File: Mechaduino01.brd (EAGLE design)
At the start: 41.9 x 41.9 mm, 64 parts, among them IC1 SAMD21G18A-AUT, IC2 AP2112K-3.3, Q1 2.5A/30V, Q2 NFET, Q3 BSS138, Q4 BSS138, U3 74AHC1G125, Y1 32,768Khz

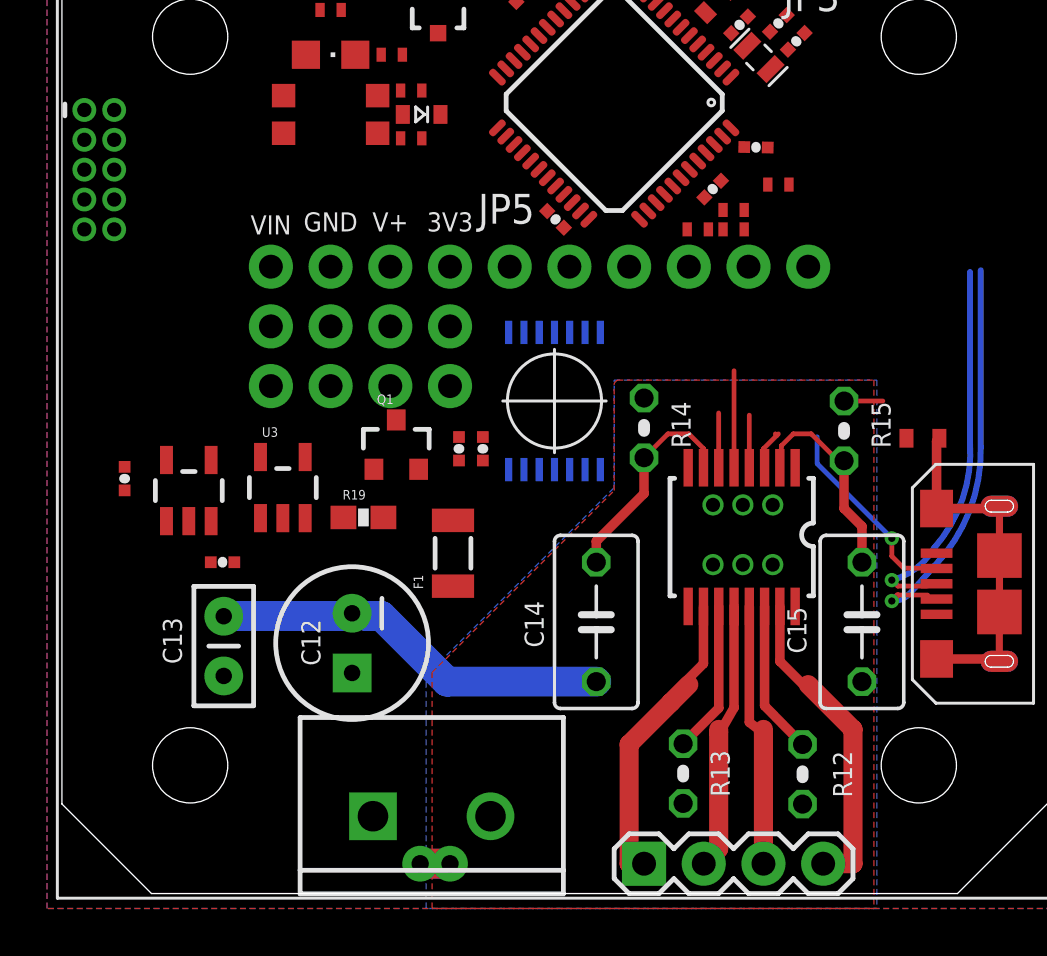
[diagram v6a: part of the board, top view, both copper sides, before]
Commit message: replaced through hole passives with smd
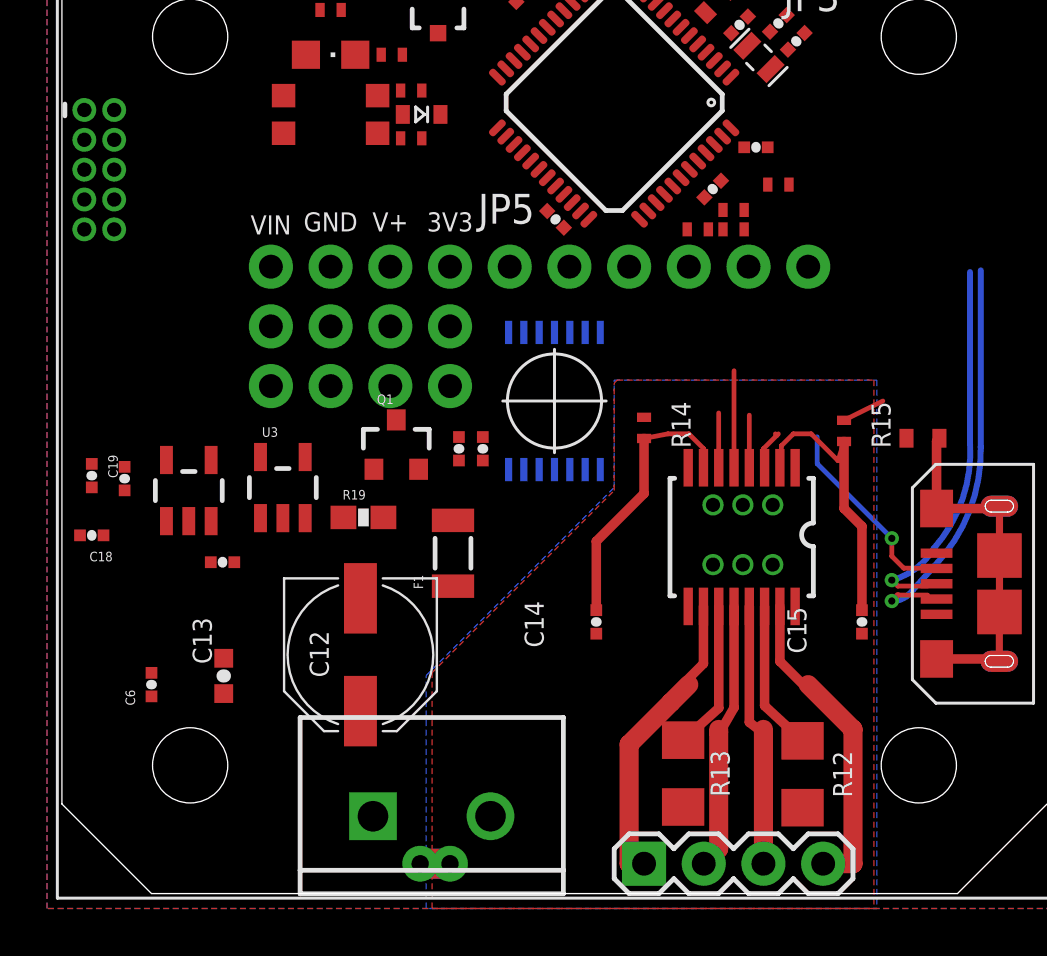
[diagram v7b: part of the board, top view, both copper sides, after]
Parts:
- added C18: 10.0uF, swift:0402-CAP
- added C19: 0.1uF, swift:0402-CAP
- added C6: 0.01uF, swift:0402-CAP
- C1, C2, C3, C4, C5: value 100nF -> 0.1uF
- C10: value 2.2uF -> 10.0uF
- C12: device SparkFun-Capacitors:CPOL-RADIAL-100UF-25V -> SparkFun-Capacitors:PANASONIC_D
- C13: value 0.22uF -> 1.0uF; device SparkFun-Capacitors:CAP-PTH-SMALLEZ -> swift:0603-CAP
- C14, C15: value (none) -> 0.1uF; device resistor:C050-035X075 -> swift:0402-CAP
- C16: value (none) -> 0.1uF
- C9: value 1uF -> 0.1uF
- L1, L2: value (none) -> BLM18PG471SN1D
- R12, R13: device resistor:0204V -> adafruit:R1206
- R14, R15: device resistor:0204V -> adafruit:R0402-VISHAY
- moved C12 0.61 mm to (12.7, 10.2)
- turned C2 to 0 degrees
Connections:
- net 3.3V: now also C19.1
- net GND: now also C18.2, C19.2
- net GND2: now also C12.-, C6.2; no longer C12.2
- net V+: now also C12.+, C6.1; no longer C12.1
- net VIN: now also C18.1
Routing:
- net GND2: track 17.1 -> 0.00 mm
- net N$6: track 8.95 -> 12.4 mm
- net N$32: track 9.32 -> 11.8 mm

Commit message: routed?
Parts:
- removed JP3: (no value), SparkFun-Connectors:1X10_NO_SILK
- removed JP5: (no value), SparkFun-Connectors:1X06_NO_SILK
- added J2: (no value), MF_Connectors:PTH_2.54MM_01X10
- added J3: (no value), MF_Connectors:PTH_2.54MM_01X06
- 3V3, GND, V+, VIN: device SparkFun-Connectors:1X03_NO_SILK -> MF_Connectors:PTH_2.54MM_01X03
- moved Q3 40.6 mm to (10.3, 31.5), turned to 0 degrees
- moved JP4 38.6 mm to (40.1, 29.0)
- moved R20 36.9 mm to (10.3, 29.3), turned to 180 degrees
- moved R21 36.2 mm to (10.9, 34.3), turned to 90 degrees
- moved R2 34.7 mm to (12.3, 34.3), turned to 90 degrees
- moved R3 34.0 mm to (13.3, 29.3), turned to 180 degrees
- moved Q4 32.4 mm to (13.3, 31.5), turned to 0 degrees
- moved U$3 21.1 mm to (49.8, 18.9), flipped to the top
- moved R9 20.8 mm to (17.8, 13.7), turned to 180 degrees
- moved C19 16.3 mm to (17.5, 18.7), turned to 0 degrees
- moved C5 16.0 mm to (10.9, 37.3), turned to 90 degrees
- moved R6 15.1 mm to (29.6, 35.6), turned to 0 degrees
- moved Q2 15.0 mm to (3.17, 29.8), flipped to the bottom, turned to 0 degrees
- moved L2 14.6 mm to (13.3, 37.3), turned to 270 degrees
- moved Y1 13.8 mm to (16.1, 38.2), flipped to the bottom, turned to 90 degrees
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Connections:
- net 3.3V: now also 3V3.P$1, 3V3.P$2, 3V3.P$3; no longer 3V3.1, 3V3.2, 3V3.3
- net ARDUINO_A0: now also J2.P$9; no longer JP3.2
- net ARDUINO_A1: now also J2.P$8; no longer JP3.3
- net ARDUINO_A3: now also J2.P$7; no longer JP3.4
- net ARDUINO_A4: now also J2.P$6; no longer JP3.5
- net ARDUINO_A5: now also J2.P$5; no longer JP3.6
- net ARDUINO_AREF: now also J2.P$10; no longer JP3.1
- net ARDUINO_D10_SS: now also J3.P$1; no longer JP5.1
- net ARDUINO_D11_MOSI: now also J3.P$2; no longer JP5.2
- net ARDUINO_D12_MISO: now also J3.P$3; no longer JP5.3
- net ARDUINO_D13_SCK: now also J3.P$4; no longer JP5.4
- net ARDUINO_D2: now also J2.P$2; no longer JP3.9
- net ARDUINO_D20_SDA: now also J3.P$5; no longer JP5.5
- net ARDUINO_D21_SCL: now also J3.P$6; no longer JP5.6
- net ARDUINO_D3: now also J2.P$1; no longer JP3.10
- net GND: now also GND.P$1, GND.P$2, GND.P$3; no longer GND.1, GND.2, GND.3
- net HV1: now also J2.P$3; no longer JP3.8
- net HV2: now also J2.P$4; no longer JP3.7
- net V+: now also V+.P$1, V+.P$2, V+.P$3; no longer V+.1, V+.2, V+.3
- net VIN: now also VIN.P$1, VIN.P$2, VIN.P$3; no longer VIN.1, VIN.2, VIN.3
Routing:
- net 3.3V: track 0.00 -> 79.8 mm, vias 0 -> 3
- net V+: track 0.00 -> 71.7 mm, vias 0 -> 2
- net RESET: track 0.00 -> 68.2 mm, vias 0 -> 3
- net VIN: track 0.00 -> 48.8 mm, vias 0 -> 3
- net ARDUINO_D13_SCK: track 0.00 -> 38.0 mm, vias 0 -> 3
- net GND2: track 0.00 -> 32.9 mm, vias 6 -> 9
- net N$7: track 8.65 -> 38.0 mm, vias 1 -> 2
- net ARDUINO_D4----VREF2: track 1.84 -> 28.3 mm, vias 0 -> 2
- net ARDUINO_D21_SCL: track 0.00 -> 23.7 mm, vias 0 -> 4
- net PA30_SWCLK: track 0.00 -> 22.6 mm, vias 0 -> 3
- net ARDUINO_D8----IN1: track 2.33 -> 24.9 mm, vias 0 -> 2
- net PA31_SWDIO: track 0.00 -> 21.3 mm
- net ARDUINO_D5----IN3: track 1.82 -> 22.2 mm, vias 0 -> 2
- net ARDUINO_D9----VREF1: track 0.00 -> 19.6 mm, vias 0 -> 2
- net N$36: track 0.00 -> 19.3 mm, vias 0 -> 1
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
